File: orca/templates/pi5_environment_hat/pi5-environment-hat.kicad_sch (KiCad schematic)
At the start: 25 parts, among them J1 Raspberry Pi 5 GPIO, J2 ALARM_OD_GND, Q1 2N7000, U1 SHT31-DIS-B2.5kS, U2 CAT24C32

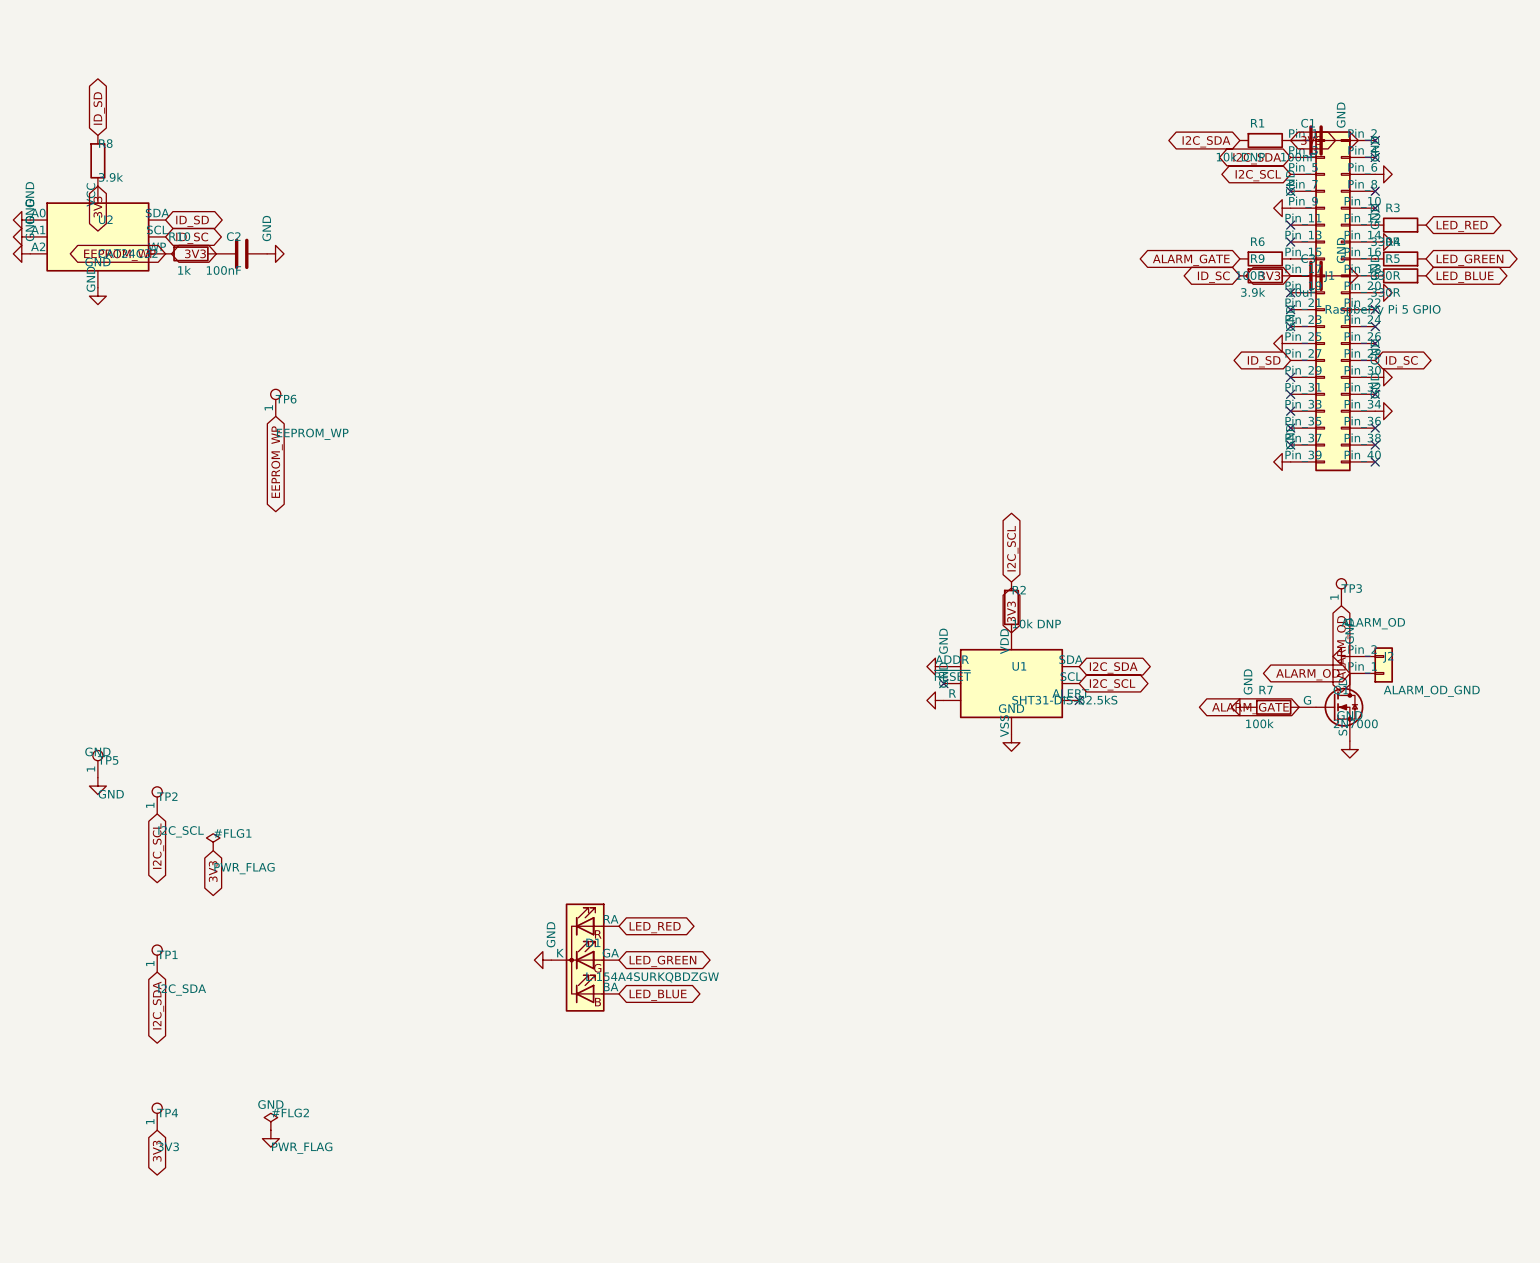
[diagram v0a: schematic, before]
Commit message: Correct environmental HAT pinout and sensor reads
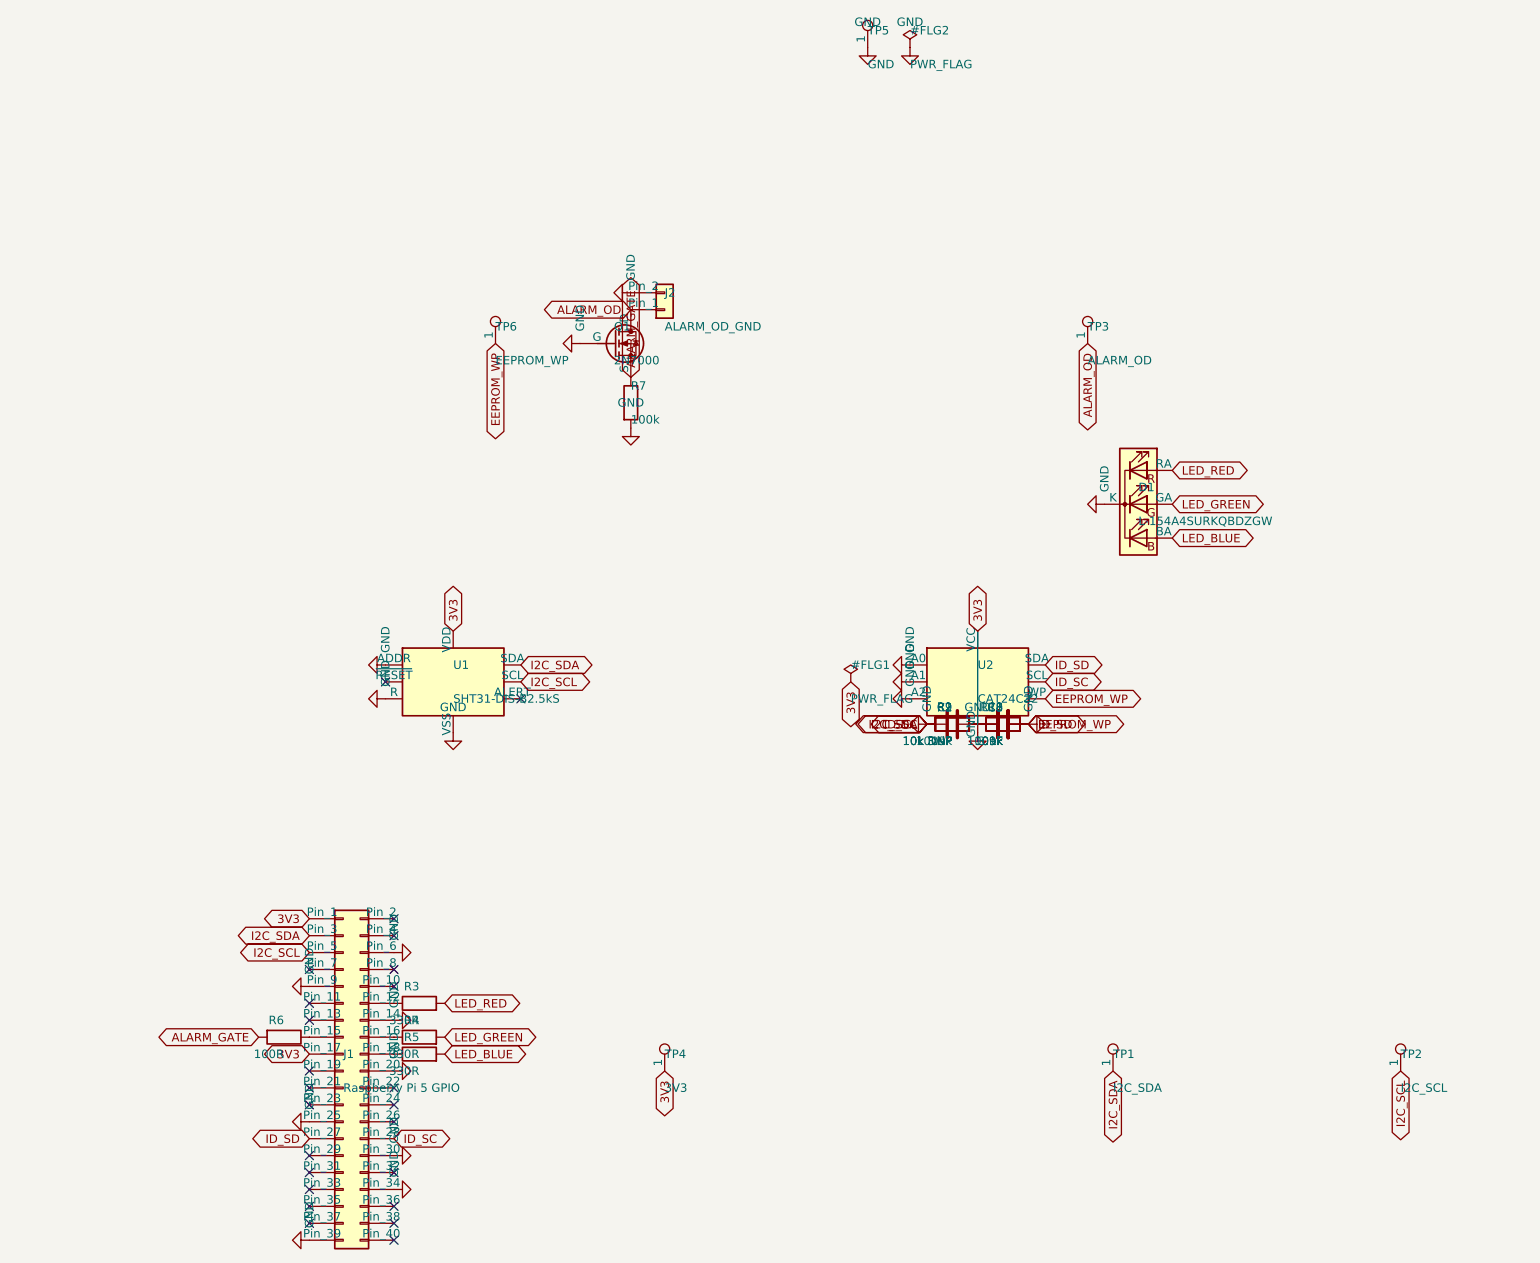
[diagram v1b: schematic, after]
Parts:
- Q1: symbol Transistor_FET:Q_NMOS_GSD -> Transistor_FET:Q_NMOS_SGD
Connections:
- net EEPROM_WP is gone; now on net GND: R10.2, TP6.1, U2.7 (WP)
- net I2C_SCL is gone; now on net GND: J1.5 (Pin_5), R2.2, TP2.1, U1.4 (SCL)
- net I2C_SDA is gone; now on net GND: J1.3 (Pin_3), R1.2, TP1.1, U1.1 (SDA)
- net ID_SC is gone; now on net GND: J1.28 (Pin_28), R9.2, U2.6 (SCL)
- net ID_SD is gone; now on net GND: J1.27 (Pin_27), R8.2, U2.5 (SDA)
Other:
- moved on the sheet: C1, C2, C3, D1, J1, J2, Q1, R1, R10, R2, R3, R4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
